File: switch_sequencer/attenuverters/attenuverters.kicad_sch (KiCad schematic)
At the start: 54 parts, among them J1 Eurorack_Power_10pin_Shrouded, J10 3.5mm_Mono_Switched_sm, J11 3.5mm_Mono_Switched_sm, J12 3.5mm_Mono_Switched_sm, J13 3.5mm_Mono_Switched_sm, J14 3.5mm_Mono_Switched_sm, J15 3.5mm_Mono_Switched_sm, J16 3.5mm_Mono_Switched_sm, J17 3.5mm_Mono_Switched_sm, J18 Conn_01x03, J19 Conn_01x03, J2 3.5mm_Mono_Switched_sm, J3 3.5mm_Mono_Switched_sm, J4 3.5mm_Mono_Switched_sm, J5 3.5mm_Mono_Switched_sm, J6 3.5mm_Mono_Switched_sm, J7 3.5mm_Mono_Switched_sm, J8 3.5mm_Mono_Switched_sm, J9 3.5mm_Mono_Switched_sm, U1 LD1117S50TR_SOT223, U2 LT1964-5, U3 LM358, U4 LM358, U5 LM358, U6 LM358

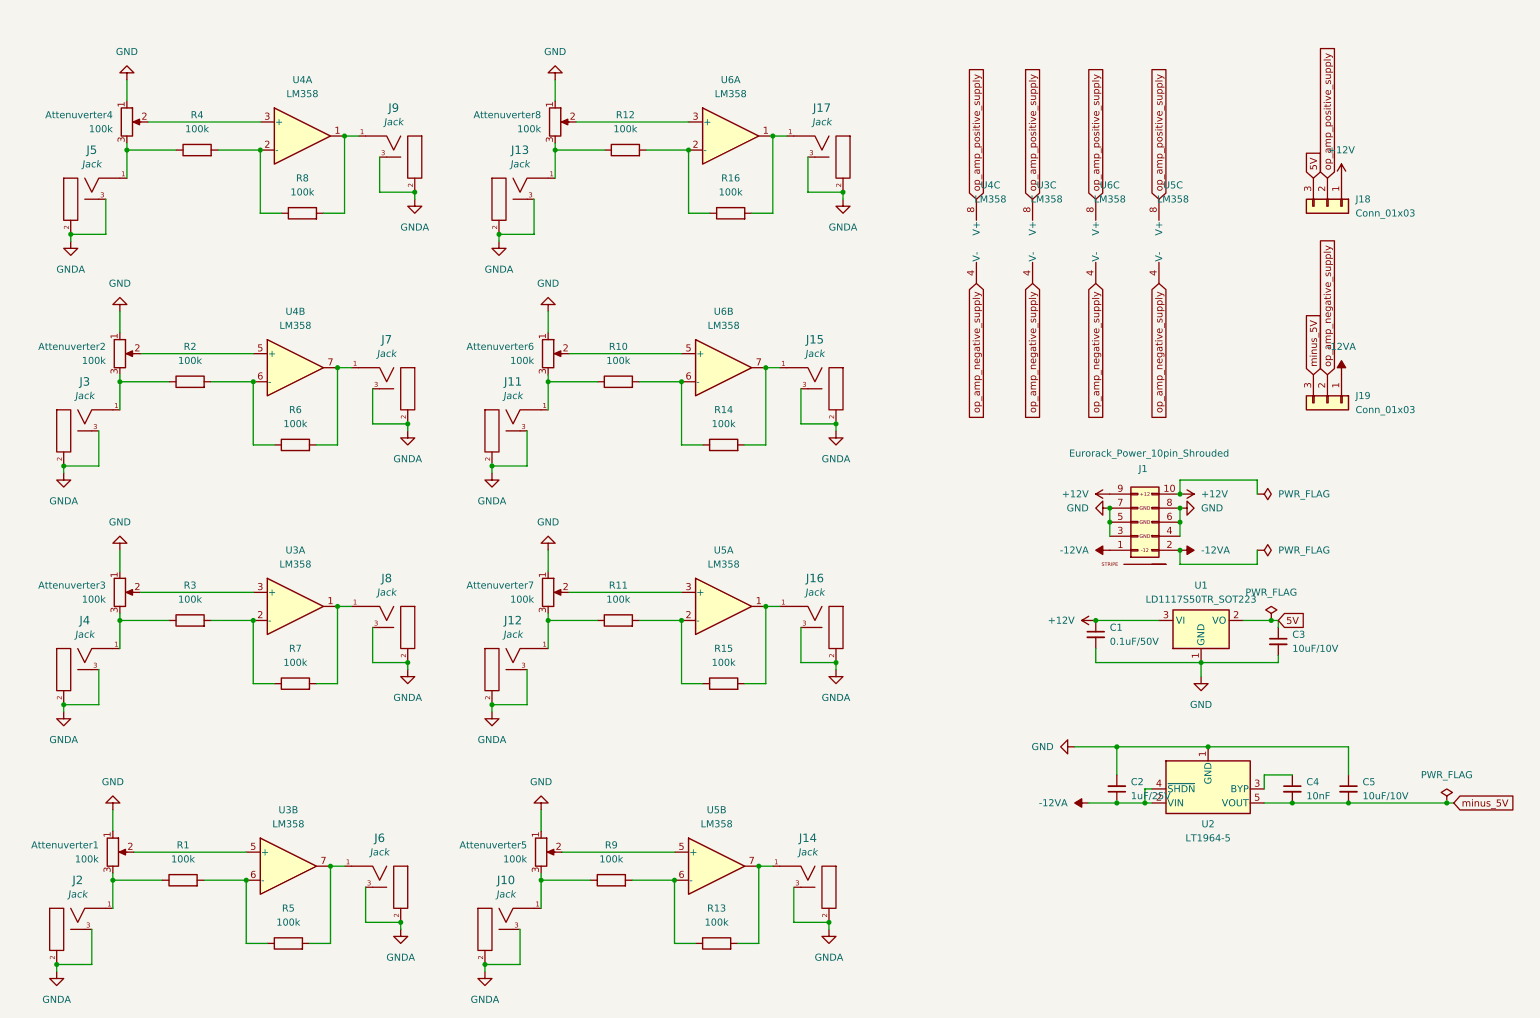
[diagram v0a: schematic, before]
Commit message: Added attenuveter PCB
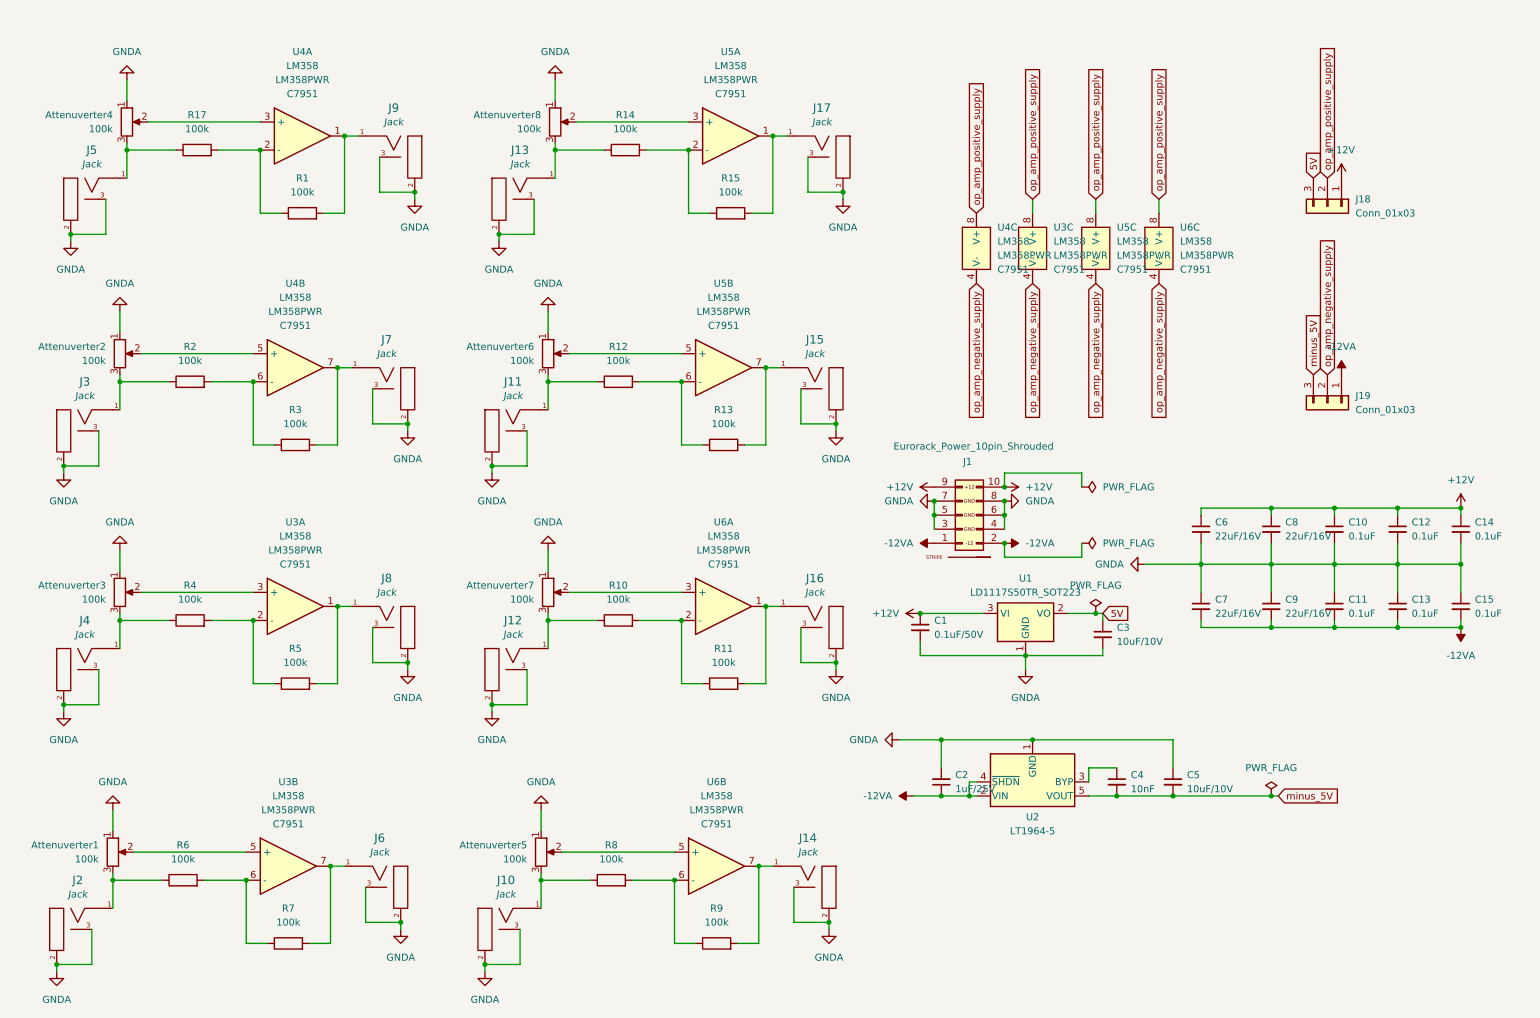
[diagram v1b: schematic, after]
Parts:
- removed R1, R10, R11, R12, R13, R14, R15, R16, R2, R3, R4, R5, R6, R7, R8, R9: 100k, Resistor_THT:R_Axial_DIN0207_L6.3mm_D2.5mm_P10.16mm_Horizontal, symbol Device:R
- removed U3, U4, U5, U6: LM358, LM358PE3:DIP794W45P254L959H508Q8, symbol Amplifier_Operational:LM358
- added C10, C11, C12, C13, C14, C15: 100nF_0603_16V, 4ms_Capacitor:C_0603, symbol 4ms_Capacitor:100nF_0603_16V
- added C6, C7, C8, C9: 22uF_0603_16V, 4ms_Capacitor:C_0805, symbol 4ms_Capacitor:22uF_0603_16V
- added R1, R10, R11, R12, R13, R14, R15, R17, R2, R3, R4, R5, R6, R7, R8, R9: 100k_0402, 4ms_Resistor:R_0402, symbol 4ms_Resistor:100k_0402
- added U3, U4, U5, U6: LM358, 4ms_Package_SSOP:TSSOP-8_4.4x3mm_Pitch0.65mm, symbol 4ms_IC:LM358
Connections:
- net GND is gone; now on net GNDA: Attenuverter1.1, Attenuverter2.1, Attenuverter3.1, Attenuverter4.1, Attenuverter5.1, Attenuverter6.1, Attenuverter7.1, Attenuverter8.1, C1.2, C2.2, C3.2, C5.1, J1.3 (GND), J1.4 (GND), J1.5 (GND), J1.6 (GND), J1.7 (GND), J1.8 (GND), U1.1 (GND), U2.1 (GND)
- net +12V: now also C10.1, C12.1, C14.1, C6.1, C8.1
- net -12VA: now also C11.2, C13.2, C15.2, C7.2, C9.2
- net GNDA: now also C10.2, C11.1, C12.2, C13.1, C14.2, C15.1, C6.2, C7.1, C8.2, C9.1
- net op_amp_negative_supply: now also U3.4 (V-), U4.4 (V-), U5.4 (V-), U6.4 (V-)
- net op_amp_positive_supply: now also U3.8 (V+), U4.8 (V+), U5.8 (V+), U6.8 (V+)
- net at Attenuverter6.2: now also U5.5 (+)
- net at Attenuverter6.3, J11.1 (SIG): now also R12.1
- net at J9.1 (SIG): now also R1.2, U4.1
- net at Attenuverter7.3, J12.1 (SIG): now also R10.1
- net at Attenuverter8.2: now also U5.3 (+)
- net at Attenuverter8.3, J13.1 (SIG): now also R14.1
- net at Attenuverter3.3, J4.1 (SIG): now also R4.1
- net at J16.1 (SIG): now also R11.2, U6.1
- net at Attenuverter4.2: now also U4.3 (+)
- net at Attenuverter2.2: now also U4.5 (+)
- net at J7.1 (SIG): now also R3.2, U4.7
- net at J15.1 (SIG): now also R13.2, U5.7
- net at Attenuverter5.3, J10.1 (SIG): now also R8.1
- net at J8.1 (SIG): now also R5.2, U3.1
- net at Attenuverter3.2: now also U3.3 (+)
- net at Attenuverter5.2: now also U6.5 (+)
- net at Attenuverter7.2: now also U6.3 (+)
- net at Attenuverter4.3, J5.1 (SIG): now also R17.1
- net at J14.1 (SIG): now also R9.2, U6.7
- net at J17.1 (SIG): now also R15.2, U5.1
- net at Attenuverter1.3, J2.1 (SIG): now also R6.1
- net at J6.1 (SIG): now also R7.2, U3.7
- net at Attenuverter1.2: now also U3.5 (+)
- net at Attenuverter2.3, J3.1 (SIG): now also R2.1
- new net: R14.2, R15.1, U5.2 (-)
- new net: R6.2, R7.1, U3.6 (-)
- new net: R10.2, R11.1, U6.2 (-)
- new net: R1.1, R17.2, U4.2 (-)
- new net: R4.2, R5.1, U3.2 (-)
- new net: R2.2, R3.1, U4.6 (-)
- new net: R12.2, R13.1, U5.6 (-)
- new net: R8.2, R9.1, U6.6 (-)
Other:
- moved on the sheet: C1, C2, C3, C4, C5, J1, U1, U2

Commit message: finish attenuverters, sample and hold
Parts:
- removed C2: 1uF_0603_25V, 4ms_Capacitor:C_0603, symbol 4ms_Capacitor:1uF_0603_25V
- removed C4: 10nF_0603_25V, 4ms_Capacitor:C_0603, symbol 4ms_Capacitor:10nF_0603_25V
- removed C5: 10uF_0603_10V, 4ms_Capacitor:C_0603, symbol 4ms_Capacitor:10uF_0603_10V
- removed J19: Conn_01x03, 4ms_Connector:Pins_1x03_2.54mm_TH, symbol 4ms_Connector:Conn_01x03
- removed U2: LT1964-5, Package_TO_SOT_SMD:TSOT-23-5, symbol Regulator_Linear:LT1964-5
- added H1, H2, H3, H4: MountingHole, 4ms_Faceplate:Faceplate_Rail_Mount_Slot_Plated, symbol Mechanical:MountingHole
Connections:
- net op_amp_negative_supply is gone; now on net -12VA: U3.4 (V-), U4.4 (V-), U5.4 (V-), U6.4 (V-)
- net +12V: now also U3.8 (V+), U4.8 (V+), U5.8 (V+), U6.8 (V+)
- net GNDA: no longer J10.3 (SW), J11.3 (SW), J12.3 (SW), J13.3 (SW), J14.3 (SW), J15.3 (SW), J16.3 (SW), J17.3 (SW), J2.3 (SW), J3.3 (SW), J4.3 (SW), J5.3 (SW), J6.3 (SW), J7.3 (SW), J8.3 (SW), J9.3 (SW)
- removed net op_amp_positive_supply: J18.2 (Pin_2), U3.8 (V+), U4.8 (V+), U5.8 (V+), U6.8 (V+)
- new net NORMALED_IN: J10.3 (SW), J11.3 (SW), J12.3 (SW), J13.3 (SW), J18.2 (Pin_2), J2.3 (SW), J3.3 (SW), J4.3 (SW), J5.3 (SW)
- no-connect marks 0 -> 8
